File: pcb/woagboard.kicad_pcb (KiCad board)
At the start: 2 copper layers, 247.7 x 97.7 mm, 95 parts, among them J1 Battery JST, J2 Flash connection, J3 Battery JST, J4 Flash connection, SW1 SW_Push, SW10 SW_Push, SW11 SW_Push, SW12 SW_Push, SW13 SW_Push, SW14 SW_Push, SW15 SW_Push, SW16 SW_Push, SW17 SW_Push, SW18 SW_Push, SW19 SW_Push, SW2 SW_Push, SW20 SW_Push, SW21 SW_Push, SW22 SW_Push, SW23 SW_Push, SW24 SW_Push, SW25 SW_Push, SW26 SW_Push, SW27 SW_Push, SW28 SW_Push, SW29 SW_Push, SW3 SW_Push, SW30 SW_Push, SW31 SW_Push, SW32 SW_Push, SW33 SW_Push, SW34 SW_Push, SW35 SW_Push, SW36 SW_Push, SW4 SW_Push, SW5 SW_Push, SW6 SW_Push, SW7 SW_Push, SW8 SW_Push, SW9 SW_Push, U1 SRV05-4, U2 SRV05-4, U3 BQ24075, U4 BQ24075, U5 nRF52840_E73-2G4M08S1C, U9 nRF52840_E73-2G4M08S1C, Y1 32.768 KHz, Y2 32.768 KHz

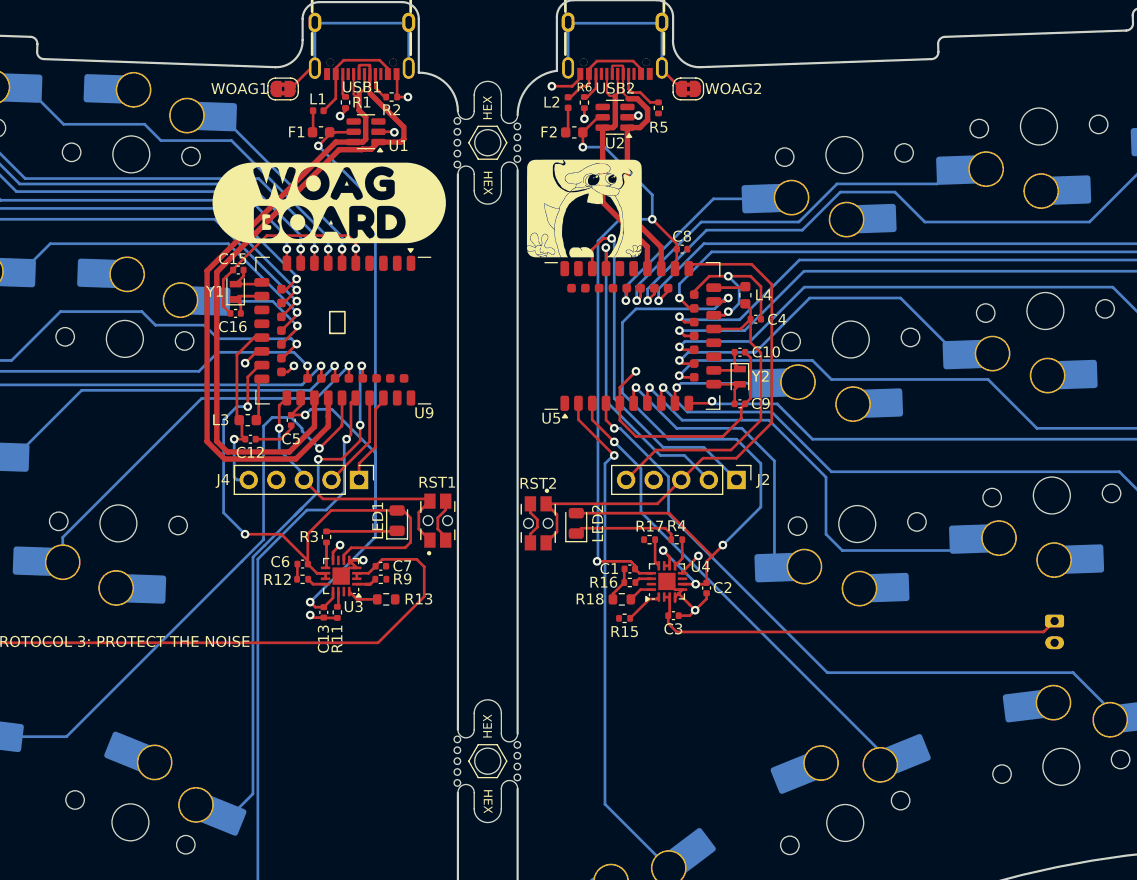
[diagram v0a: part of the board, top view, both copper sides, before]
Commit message: feat: better usb trace impedance and silkscreen shenangains
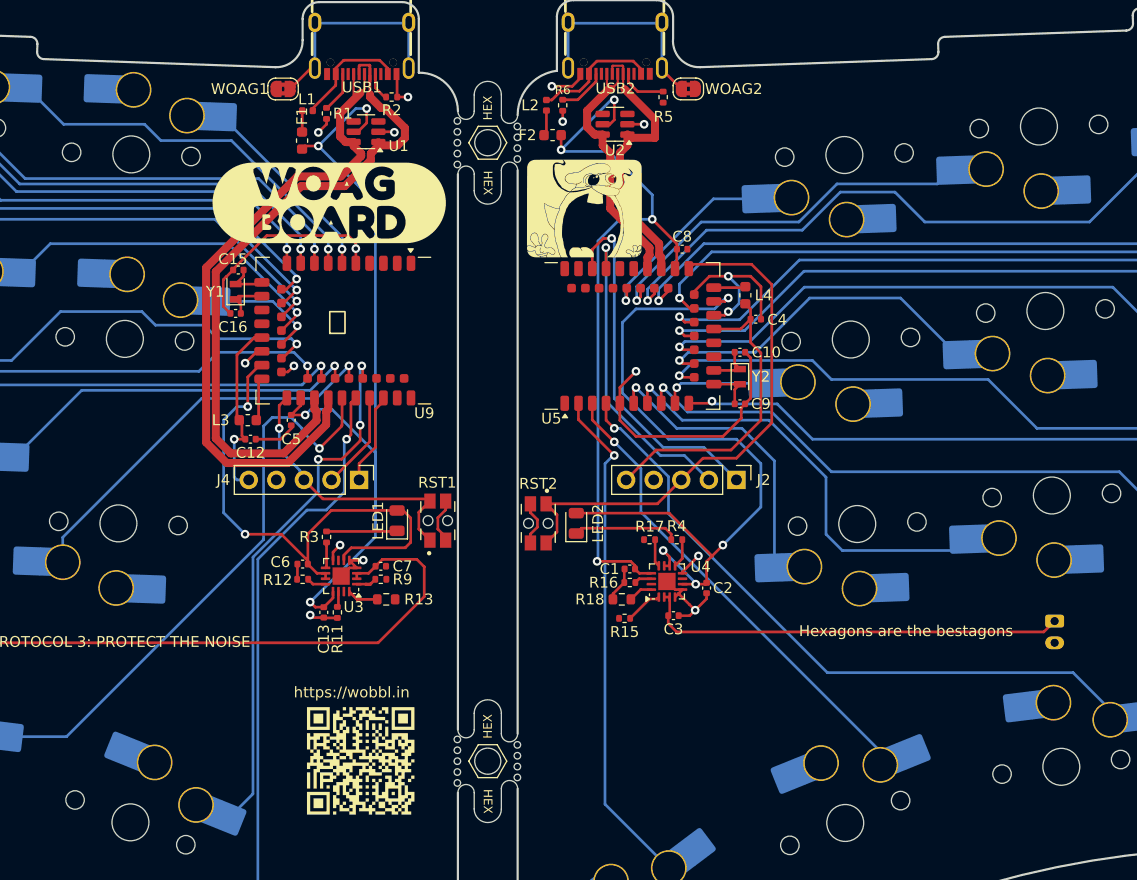
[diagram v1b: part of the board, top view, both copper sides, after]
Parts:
- added ?: , clipboard:b0b166cb-dd6f-4d51-8f1e-dffc821eec14, F.Cu at (127.8, 100.1)
- added ?: , clipboard:f1388248-bc64-4771-8030-6004cabea107, B.Cu at (132.3, 99.8)
- added G***: LOGO, LOGO, B.Cu at (67.8, 77.9)
- added G***: LOGO, LOGO, B.Cu at (210.6, 87.3)
- added G***: LOGO, LOGO, B.Cu at (222.0, 87.5)
- moved R1 2.02 mm to (127.0, 35.5)
- moved F2 2.02 mm to (147.8, 37.5)
- moved L2 2.02 mm to (147.2, 34.8)
- moved R6 2.02 mm to (148.8, 34.8)
- moved F1 1.91 mm to (124.8, 38.0), turned to -90 degrees
- moved R5 1.08 mm to (158.0, 34.0)
- moved L1 1.00 mm to (125.2, 35.2)
- moved U2 0.64 mm to (153.6, 36.5)
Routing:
- net +5V: track 133.3 -> 149.3 mm, vias 6 -> 8
- net USB-D+: track 59.4 -> 62.1 mm
- net VBUS: track 20.1 -> 22.6 mm
- net Net-(USB2-CC2): track 2.81 -> 4.91 mm
- net Net-(USB1-CC2): track 1.80 -> 3.77 mm
- net USB-R-D-: track 25.2 -> 26.5 mm
- net Switch17: track 50.2 -> 49.2 mm
- net USB-D-: track 61.5 -> 62.5 mm
- net GND: track 110.6 -> 111.3 mm
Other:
- board text added: "Hexagons are the bestagons"
- board text added: "SUPER MURDER"
- board text added: "https://wobbl.in"

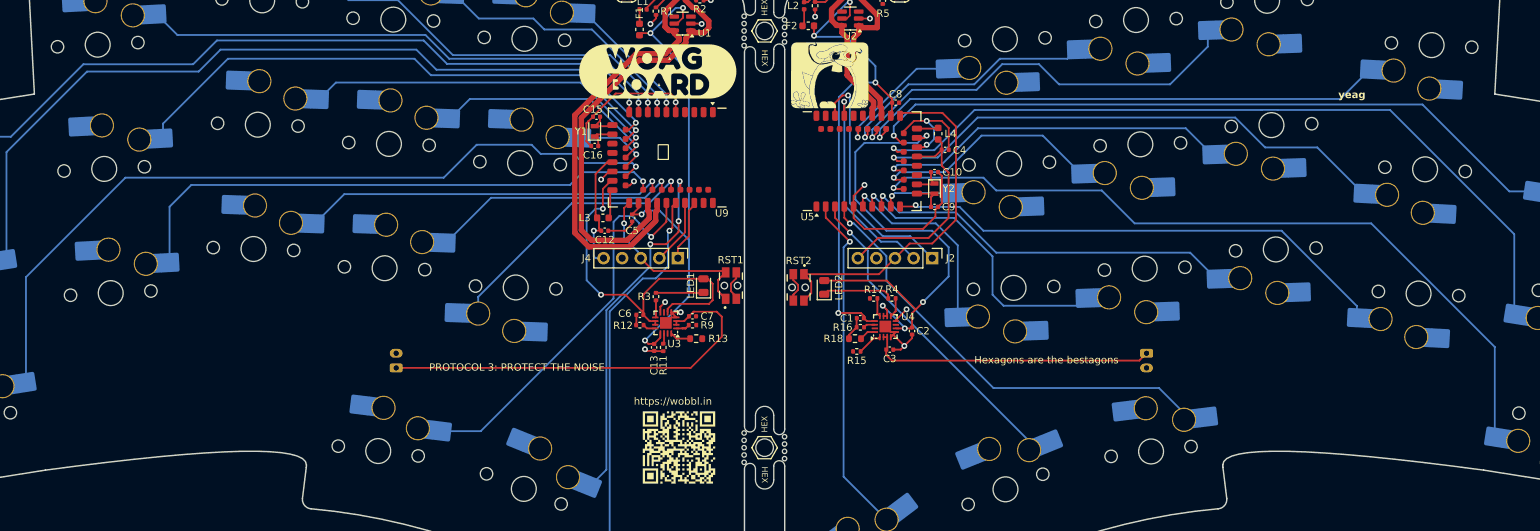
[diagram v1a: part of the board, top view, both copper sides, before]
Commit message: chore: more silkscreen stuffs
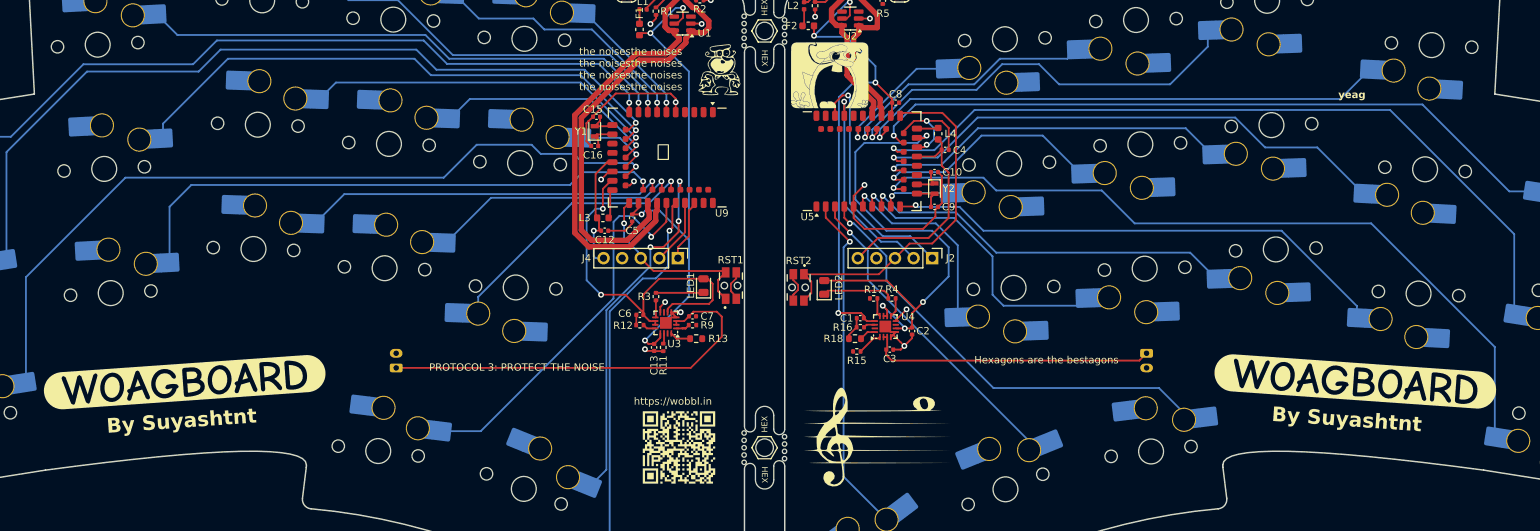
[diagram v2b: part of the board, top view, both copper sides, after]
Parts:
- removed kibuzzard-66E410C5: G***, kibuzzard-66E410C5
- added G***: LOGO, LOGO, F.Cu at (157.2, 93.8)
- added G***: LOGO, LOGO, F.Cu at (135.8, 41.4)
- added G***: LOGO, LOGO, B.Cu at (127.6, 57.5)
- added kibuzzard-66E93FFE: G***, kibuzzard-66E93FFE, F.Cu at (62.6, 86.2)
- added kibuzzard-66E93FFE: G***, kibuzzard-66E93FFE, F.Cu at (222.6, 86.1)
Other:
- board text added: "By Suyashtnt"
- board text added: "the noisesthe noises the noisesthe noises the noisesthe noises the noisesthe noises"

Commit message: feat: RC1
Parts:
- removed ?: , clipboard:b0b166cb-dd6f-4d51-8f1e-dffc821eec14
- removed ?: , clipboard:f1388248-bc64-4771-8030-6004cabea107
- U3, U4: footprint Package_DFN_QFN:VQFN-16-1EP_3x3mm_P0.5mm_EP1.6x1.6mm -> SamacSys_Parts:QFN50P300X300X80-17N-D
